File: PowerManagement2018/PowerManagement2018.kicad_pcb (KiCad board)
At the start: 2 copper layers, 46.4 x 27.3 mm, 25 parts, among them J1 Conn_01x02_Male, J2 Conn_01x02_Male, J3 Conn_01x02_Male, J4 Conn_01x02_Male, Q1 Q_PMOS_GSD

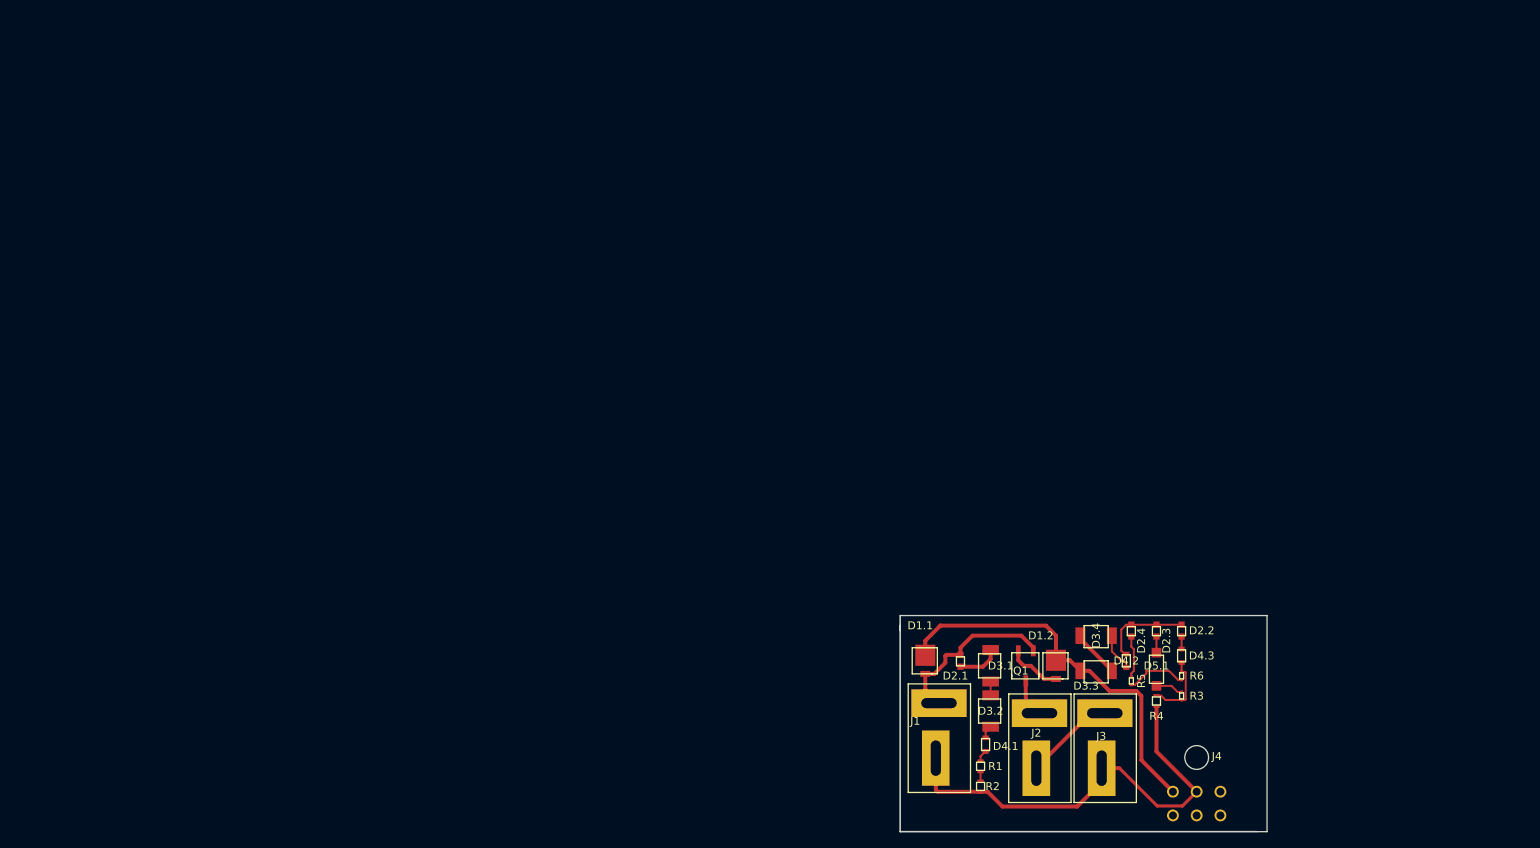
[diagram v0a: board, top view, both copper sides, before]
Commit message: Combined system
Battery charging system and battery switching system combined
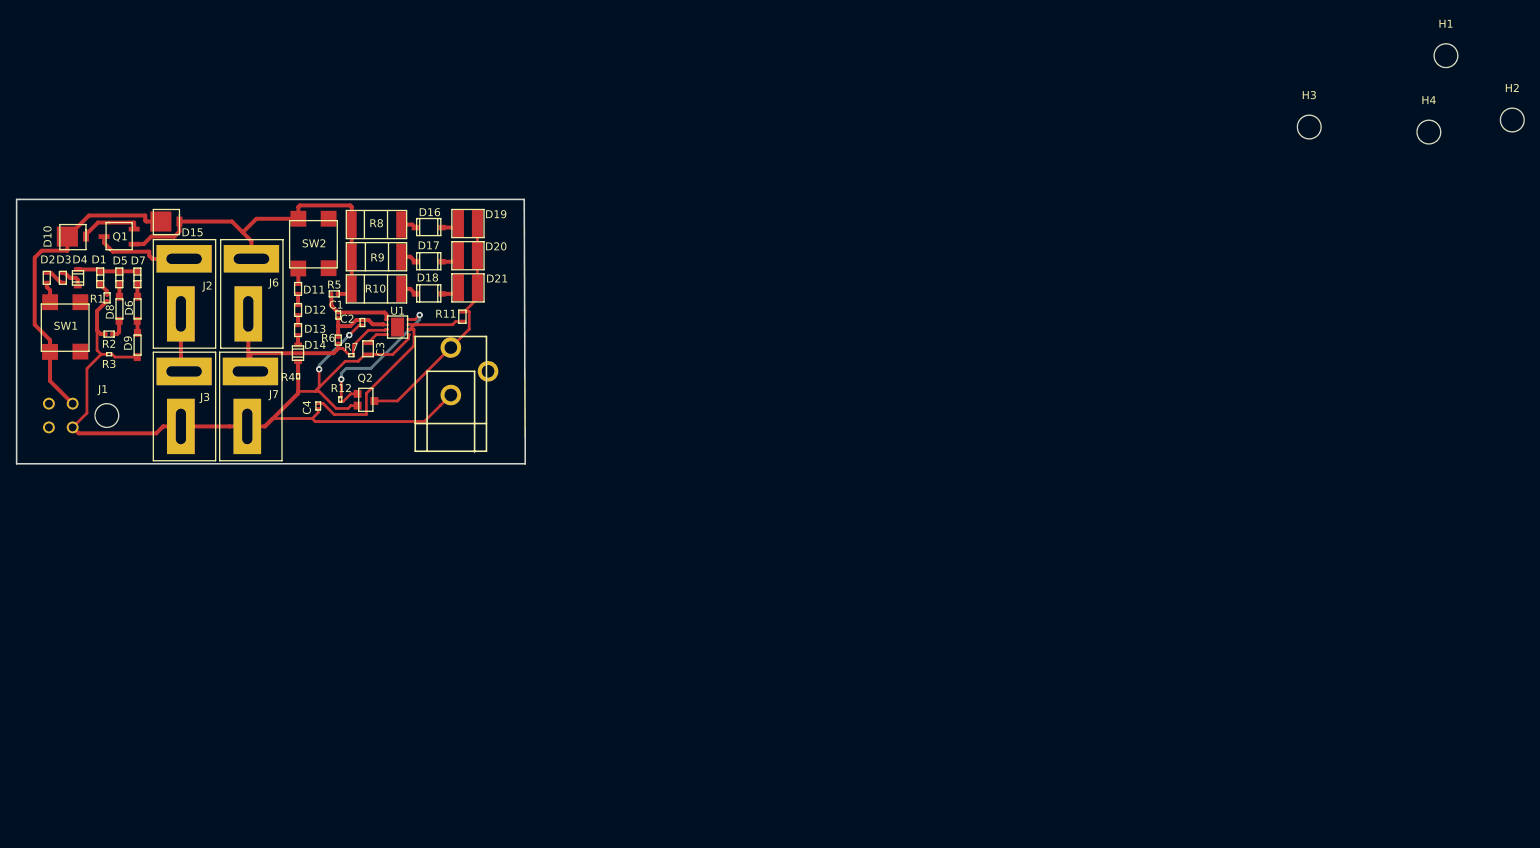
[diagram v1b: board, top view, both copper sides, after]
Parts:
- removed D1.1, D1.2: DIODE, PowerManagementBoard:UPS115U (Diode 0.22V)
- removed D2.1, D2.2, D2.3, D2.4: LED, PowerManagementBoard:LTST-C191KFKT(LED 2V)
- removed D3.1, D3.2, D3.3, D3.4: DIODE, PowerManagementBoard:CD214A-R150_R11600(Diode 2V)
- removed D4.1, D4.2, D4.3: DIODE, PowerManagementBoard:CES388(Diode 0.6V)
- removed D5.1: DIODE, PowerManagementBoard:MBR120VLSF(Diode 0.3V)
- removed J4: Conn_01x02_Male, SOAR_Kicad_Library-master:Molex_Micro-Fit_3.0_43045-0600_2x03_P3.00mm_Horizontal
- added C1: 0.1uF, New_Library:CL05B104KP5NNNC (0.1uF), F.Cu at (133.5, 92.8)
- added C2: 0.1uF, New_Library:CL05B104KP5NNNC (0.1uF), F.Cu at (136.5, 93.8)
- added C3: 0.33uF, New_Library:CL21B334KBFNNNE (0.33uF), F.Cu at (137.3, 97.2)
- added C4: 0.1uF, New_Library:CL05B104KP5NNNC (0.1uF), F.Cu at (130.9, 104.3)
- added D1: 2.05V, New_Library:SML-D12U1WT86 (2.05V 10mA), F.Cu at (103.4, 88.1)
- added D10: 220mV, New_Library:UPS115U (Diode 0.22V), F.Cu at (100.6, 82.9)
- added D11: 2.05V, New_Library:LTST-C190KFKT (2.05V 30mA), F.Cu at (128.4, 89.5)
- added D12: 2.05V, New_Library:LTST-C190KFKT (2.05V 30mA), F.Cu at (128.4, 92.2)
- added D13: 2.05V, New_Library:LTST-C190KFKT (2.05V 30mA), F.Cu at (128.4, 94.7)
- added D14: 440mV, New_Library:BAT42WS-7-F (0.44V 30mA), F.Cu at (128.4, 97.7)
- added D15: 220mV, New_Library:UPS115U (Diode 0.22V), F.Cu at (112.4, 81.0)
- added D16: 215mV, New_Library:PMEG1020EH (215mV diode), F.Cu at (144.9, 81.8)
- added D17: 215mV, New_Library:PMEG1020EH (215mV diode), F.Cu at (144.9, 86.1)
- added D18: 215mV, New_Library:PMEG1020EH (215mV diode), F.Cu at (144.9, 90.2)
- added D19: 2.4V, New_Library:XZMYH160S (2.5V LED), F.Cu at (149.9, 81.3)
- added D2: 2.05V, New_Library:LTST-C190KFKT (2.05V 30mA), F.Cu at (96.6, 88.1)
- added D20: 2.4V, New_Library:XZMYH160S (2.5V LED), F.Cu at (149.9, 85.3)
- added D21: 2.4V, New_Library:XZMYH160S (2.5V LED), F.Cu at (149.9, 89.4)
- added D3: 2.05V, New_Library:LTST-C190KFKT (2.05V 30mA), F.Cu at (98.7, 88.1)
- added D4: 440mV, New_Library:BAT42WS-7-F (0.44V 30mA), F.Cu at (100.6, 88.1)
- added D5: 2.05V, New_Library:SML-D12U1WT86 (2.05V 10mA), F.Cu at (105.8, 88.1)
- added D6: 400mV, New_Library:BAT46W-E3-08(0.4V10mA), F.Cu at (105.4, 92.1)
- added D7: 2.05V, New_Library:SML-D12U1WT86 (2.05V 10mA), F.Cu at (108.1, 88.1)
- added D8: 400mV, New_Library:BAT46W-E3-08(0.4V10mA), F.Cu at (107.7, 92.1)
- added D9: 400mV, New_Library:BAT46W-E3-08(0.4V10mA), F.Cu at (107.7, 96.6)
- added H1: MountingHole, MountingHole:MountingHole_3mm, F.Cu at (273.4, 60.1)
- added H2: MountingHole, MountingHole:MountingHole_3mm, F.Cu at (281.8, 68.2)
- added H3: MountingHole, MountingHole:MountingHole_3mm, F.Cu at (256.2, 69.1)
- added H4: MountingHole, MountingHole:MountingHole_3mm, F.Cu at (271.3, 69.7)
- added J6: Primary, New_Library:deans connector, F.Cu at (119.5, 86.7)
- added J7: Primary, New_Library:deans connector, F.Cu at (119.4, 101.0)
- added J8: Barrel_Jack_INPUT, SOAR_Kicad_Library-master:CUI_PJ-102A_2.5mm_DC_JACK, F.Cu at (147.7, 99.9)
- added Q2: Q_NMOS_DGS, New_Library:AO3414 (nmos), F.Cu at (136.9, 104.0)
- added R10: 5.9, New_Library:CRCW25125R90FKEGHP(5.9 ohms), F.Cu at (138.3, 89.5)
- added R11: 100, New_Library:RT0603(resistors), F.Cu at (148.7, 93.1)
- added R12: 1K, New_Library:RC0201(resistors), F.Cu at (133.7, 103.5)
- added R7: 100, New_Library:RC0201(resistors), F.Cu at (135.1, 97.9)
- added R8: 5.9, New_Library:CRCW25125R90FKEGHP(5.9 ohms), F.Cu at (138.3, 81.4)
- added R9: 5.9, New_Library:CRCW25125R90FKEGHP(5.9 ohms), F.Cu at (138.3, 85.5)
- added SW1: SW_Push, New_Library:1301.9320 (button), F.Cu at (97.2, 96.1)
- added SW2: SW_Push, New_Library:1301.9320 (button), F.Cu at (128.5, 85.6)
- added U1: BQ2920, New_Library:bq29209, F.Cu at (141.0, 94.4)
- J1: value Conn_01x02_Male -> OUTPUT; footprint PowerManagementBoard:deans connector -> SOAR_Kicad_Library-master:Molex_Micro-Fit_3.0_43045-0400_2x02_P3.00mm_Horizontal
- J2, J3: value Conn_01x02_Male -> Secondary; footprint PowerManagementBoard:deans connector -> New_Library:deans connector
- R1: value 30k -> 280; footprint PowerManagementBoard:RT0603DRD0730KL(30K resistors) -> New_Library:RC0402(resistors)
- R2: value 30k -> 240; footprint PowerManagementBoard:RT0603DRD0730KL(30K resistors) -> New_Library:RC0402(resistors)
- R3: value 10k -> 200; footprint PowerManagementBoard:RMCF0201(resistor 10k) -> New_Library:RC0201(resistors)
- R4: value 30k -> 100; footprint PowerManagementBoard:RT0603DRD0730KL(30K resistors) -> New_Library:RC0201(resistors)
- R5: value 10k -> 160; footprint PowerManagementBoard:RMCF0201(resistor 10k) -> New_Library:RC0402(resistors)
- R6: value 10k -> 260; footprint PowerManagementBoard:RMCF0201(resistor 10k) -> New_Library:RC0402(resistors)
- moved R3 142.2 mm to (104.5, 97.8), turned to 180 degrees
- moved Q1 126.7 mm to (105.8, 82.9), turned to 90 degrees
- moved R1 125.5 mm to (104.3, 90.2), turned to 270 degrees
- moved J3 124.1 mm to (111.0, 101.0)
- moved R2 123.6 mm to (105.0, 95.2), turned to 180 degrees
- moved J2 122.4 mm to (111.0, 86.7)
- moved R4 116.0 mm to (128.4, 100.6), turned to 270 degrees
- moved R6 114.9 mm to (133.5, 95.5)
- moved R5 112.4 mm to (132.5, 90.2), turned to 0 degrees
- moved J1 104.4 mm to (108.8, 105.5), turned to 90 degrees
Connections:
- J1 pad 1: Net-(D1.1-Pad1) -> Net-(D10-Pad2)
- J1 pad 2: GND -> GNDS
- J3 pad 2: GND -> GNDS
- Q1 pad 1: Net-(D1.1-Pad1) -> Net-(D15-Pad1)
- R1 pad 2: Net-(R1-Pad2) -> GNDS
- R2 pad 1: Net-(R1-Pad2) -> Net-(D6-Pad2)
- R2 pad 2: GND -> GNDS
- R3 pad 2: Net-(D4.3-Pad2) -> GNDS
- R4 pad 1: Net-(D4.3-Pad2) -> Net-(D14-Pad2)
- R4 pad 2: GND -> GNDS
- R5 pad 2: Net-(R5-Pad2) -> Net-(D15-Pad1)
- R6 pad 1: Net-(R5-Pad2) -> Net-(C1-Pad2)
- R6 pad 2: Net-(D4.3-Pad2) -> Net-(J6-Pad2)
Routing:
- net GNDS: track 0.00 -> 116.8 mm, vias 0 -> 2
- net GND: track 56.5 -> 0.00 mm
- net Net-(D1.1-Pad2): track 49.7 -> 0.00 mm
- net Net-(D15-Pad1): track 0.00 -> 48.6 mm
- net Net-(D10-Pad2): track 0.00 -> 40.3 mm
- net Net-(D19-Pad2): track 0.00 -> 30.9 mm
- net Net-(C4-Pad1): track 0.00 -> 28.9 mm
- net Net-(J6-Pad2): track 0.00 -> 23.3 mm
- net Net-(D1.1-Pad1): track 22.4 -> 0.00 mm
- net Net-(R12-Pad2): track 0.00 -> 18.0 mm, vias 0 -> 2
- net Net-(D2.2-Pad2): track 11.5 -> 0.00 mm
- net Net-(D4.3-Pad2): track 9.09 -> 0.00 mm
- net Net-(C1-Pad2): track 0.00 -> 8.77 mm
- net Net-(R5-Pad2): track 7.74 -> 0.00 mm
- net Net-(D1-Pad2): track 0.00 -> 7.60 mm
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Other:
- board size 46.4 x 27.3 mm -> 64.3 x 33.4 mm
- net class Default: trace_width 0.5 -> 0.35
